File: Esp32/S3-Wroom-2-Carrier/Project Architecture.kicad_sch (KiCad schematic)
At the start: 0 parts

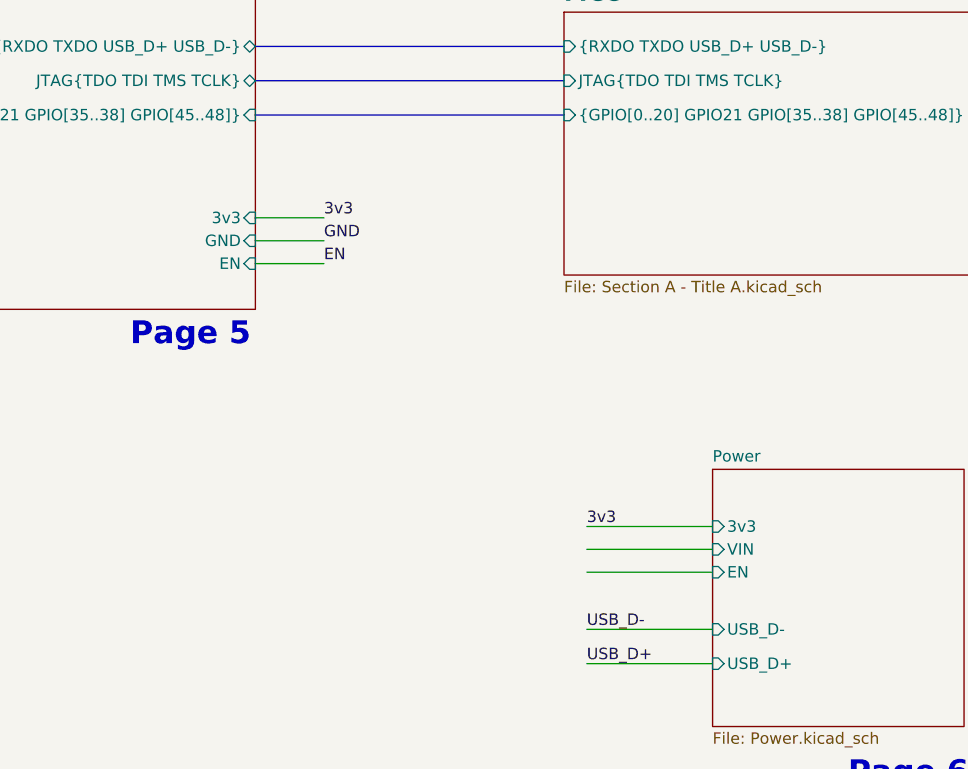
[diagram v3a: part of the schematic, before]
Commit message: Connectors
change one connector from 21 to 25 pins
Added test points
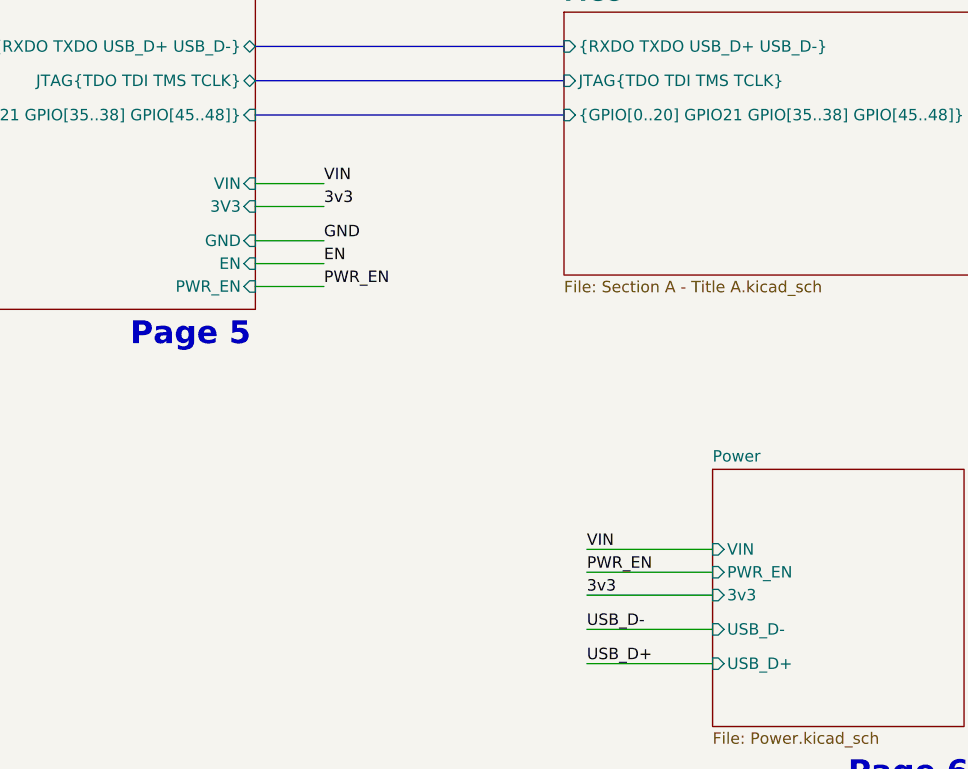
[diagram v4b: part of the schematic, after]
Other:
- sheet Break Out Connection ports: added 3V3, PWR_EN, VIN; removed 3v3
- sheet Power ports: added PWR_EN; removed EN
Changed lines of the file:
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@@
+	(wire
+		(pts
+			(xy 128.27 116.84) (xy 135.89 116.84)
+		)
+		(stroke
+			(width 0)
+			(type default)
+		)
+	)
 	(wire
 		(pts
@@
 	(wire
 		(pts
+			(xy 128.27 114.3) (xy 135.89 114.3)
+		)
+		(stroke
+			(width 0)
+			(type default)
+		)
+	)
+	(wire
+		(pts
 			(xy 223.52 115.57) (xy 231.14 115.57)
 		)
@@
 	(wire
 		(pts
+			(xy 165.1 160.02) (xy 179.07 160.02)
+		)
+		(stroke
+			(width 0)
+			(type default)
+		)
+	)
+	(wire
+		(pts
+			(xy 128.27 125.73) (xy 135.89 125.73)
+		)
+		(stroke
+			(width 0)
+			(type default)
+		)
+	)
+	(wire
+		(pts
 			(xy 128.27 120.65) (xy 135.89 120.65)
 		)
@@
 		)
 	)
-	(wire
-		(pts
-			(xy 165.1 152.4) (xy 179.07 152.4)
-		)
-		(stroke
-			(width 0)
-			(type default)
-		)
-	)
-	(wire
-		(pts
-			(xy 128.27 118.11) (xy 135.89 118.11)
-		)
-		(stroke
-			(width 0)
-			(type default)
+	(label "PWR_EN"
+		(at 135.89 125.73 0)
+		(effects
+			(font
+				(size 1.27 1.27)
+			)
+			(justify left bottom)
 		)
 	)
@@
 		)
 	)
+	(label "PWR_EN"
+		(at 165.1 157.48 0)
+		(effects
+			(font
+				(size 1.27 1.27)
+			)
+			(justify left bottom)
+		)
+	)
 	(label "USB_D-"
 		(at 165.1 163.83 0)
@@
 		)
 	)
-	(label "3v3"
-		(at 165.1 152.4 0)
+	(label "VIN"
+		(at 165.1 154.94 0)
 		(effects
 			(font
@@
 		)
 	)
-	(label "3v3"
-		(at 135.89 118.11 0)
+	(label "VIN"
+		(at 135.89 114.3 0)
 		(effects
 			(font
@@
 	(label "GND"
 		(at 135.89 120.65 0)
+		(effects
+			(font
+				(size 1.27 1.27)
+			)
+			(justify left bottom)
+		)
+	)
+	(label "3v3"
+		(at 165.1 160.02 0)
+		(effects
+			(font
+				(size 1.27 1.27)
+			)
+			(justify left bottom)
+		)
+	)
+	(label "3v3"
+		(at 135.89 116.84 0)
 		(effects
 			(font
@@
 			)
 		)
-		(pin "3v3" input
-			(at 179.07 152.4 180)
-			(effects
-				(font
-					(size 1.27 1.27)
-				)
-				(justify left)
-			)
-		)
-		(pin "EN" input
-			(at 179.07 157.48 180)
-			(effects
-				(font
-					(size 1.27 1.27)
-				)
-				(justify left)
-			)
-		)
 		(pin "VIN" input
 			(at 179.07 154.94 180)
@@
 		(pin "USB_D+" input
 			(at 179.07 167.64 180)
+			(effects
+				(font
+					(size 1.27 1.27)
+				)
+				(justify left)
+			)
+		)
+		(pin "PWR_EN" input
+			(at 179.07 157.48 180)
+			(effects
+				(font
+					(size 1.27 1.27)
+				)
+				(justify left)
+			)
+		)
+		(pin "3v3" input
+			(at 179.07 160.02 180)
 			(effects
 				(font
@@
 			)
 		)
-		(pin "3v3" input
-			(at 128.27 118.11 0)
-			(effects
-				(font
-					(size 1.27 1.27)
-				)
-				(justify right)
-			)
-		)
 		(pin "JTAG{TDO TDI TMS TCLK}" bidirectional
 			(at 128.27 102.87 0)
@@
 			(effects
 				(font
+					(size 1.27 1.27)
+				)
+				(justify right)
+			)
+		)
+		(pin "VIN" input
+			(at 128.27 114.3 0)
+			(effects
+				(font
+					(size 1.27 1.27)
+				)
+				(justify right)
+			)
+		)
+		(pin "3V3" input
+			(at 128.27 116.84 0)
+			(effects
+				(font
+					(size 1.27 1.27)
+				)
+				(justify right)
+			)
+		)
+		(pin "PWR_EN" input
+			(at 128.27 125.73 0)
+			(effects
+				(font
